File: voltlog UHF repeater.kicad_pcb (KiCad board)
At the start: 4 copper layers, 48.2 x 46.2 mm, 38 parts, among them J1 Conn_02x13_Odd_Even, J2 Conn_01x13, J3 Conn_Coaxial, Q1 Q_NPN_BEC, Q2 Q_PNP_BEC, U1 SA818

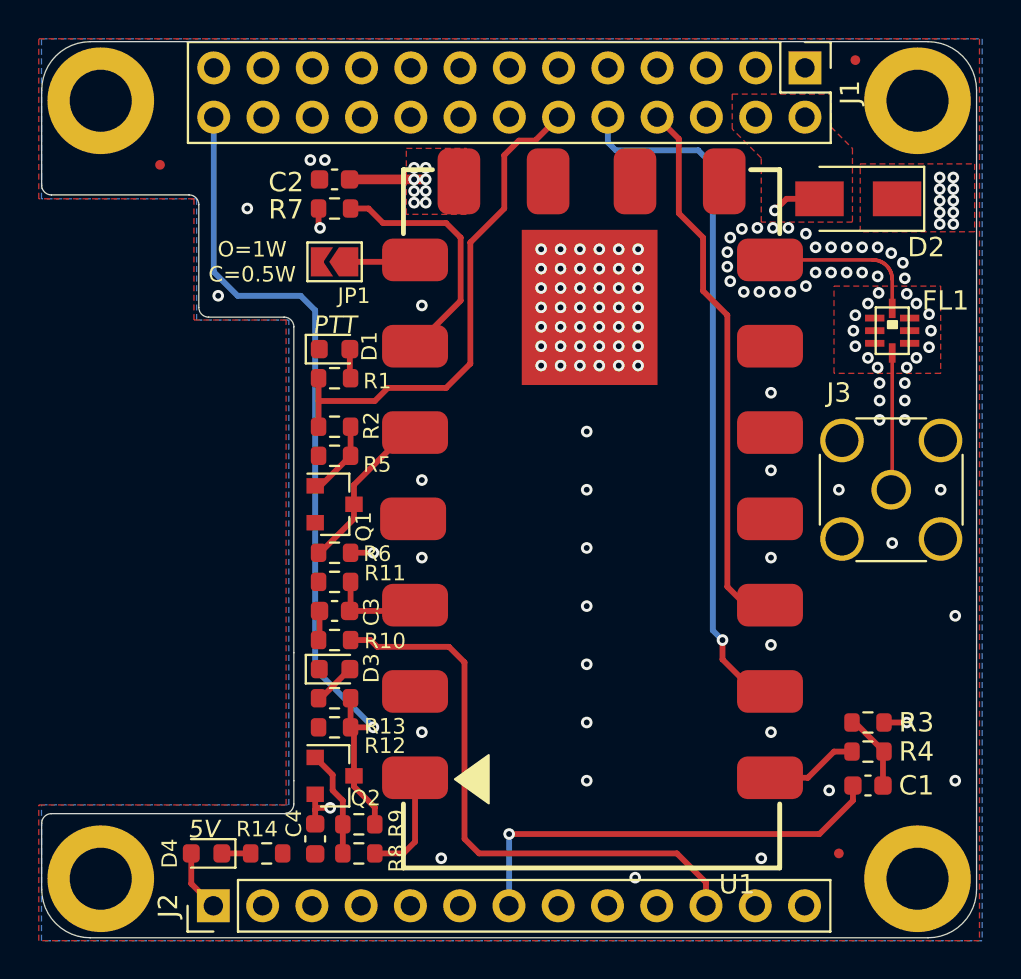
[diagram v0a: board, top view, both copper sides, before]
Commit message: Added pulldown for MIC1N. Added part no for JLCPCB and production files for JLCPCB.
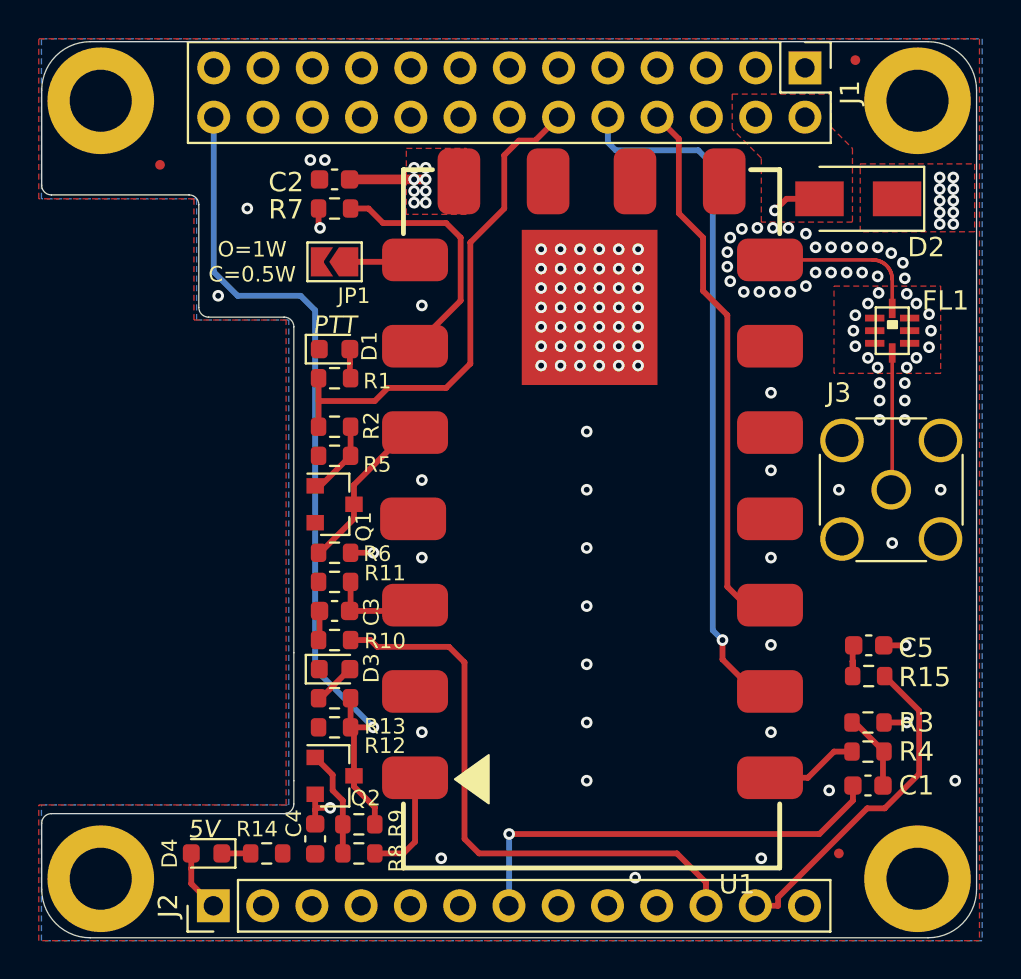
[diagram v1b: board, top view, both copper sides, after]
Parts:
- removed V1: VOLTLOG_LOGO, Voltlog:voltlog_mask_3mm
- added C5: 470nF, Capacitor_SMD:C_0603_1608Metric, F.Cu at (201.5, 65.0)
- added R15: 2K2, Resistor_SMD:R_0603_1608Metric, F.Cu at (201.5, 66.6)
- D1: value PTT -> LED
- D3: value SQL -> LED
- D4: value 5V -> LED
- Q1: value Q_NPN_BEC -> BC847
- Q2: value Q_PNP_BEC -> BC857
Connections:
- FL1 pad 2: Net-(FL1-Pad2) -> unconnected-(FL1-NC-Pad2)
- FL1 pad 6: Net-(FL1-Pad6) -> unconnected-(FL1-NC-Pad6)
- J2 pad 12: /MIC1N -> MIC1N
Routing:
- net MIC1N: track 0.00 -> 17.3 mm
- net Net-(C5-Pad1): track 0.00 -> 2.37 mm
- net GND: track 1.18 -> 2.31 mm
- net +5V: track 74.0 -> 74.8 mm
- net Net-(D1-A): track 1.46 -> 2.25 mm
- added copper zone on In1.Cu, net GND
- added copper zone on In2.Cu, net GND
- added copper zone on In2.Cu, net Net-(D2-K)
- removed copper zone on GND.Cu, net GND
- removed copper zone on PWR.Cu, net GND
- removed copper zone on PWR.Cu, net Net-(D2-K)
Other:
- net class 50ohm removed
- net class Default removed
- board text added: "revB"
- board text removed: "UHF"
- board text removed: "revA 3721"

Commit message: Fixed errors caused by orangepi outline present in Margin layer
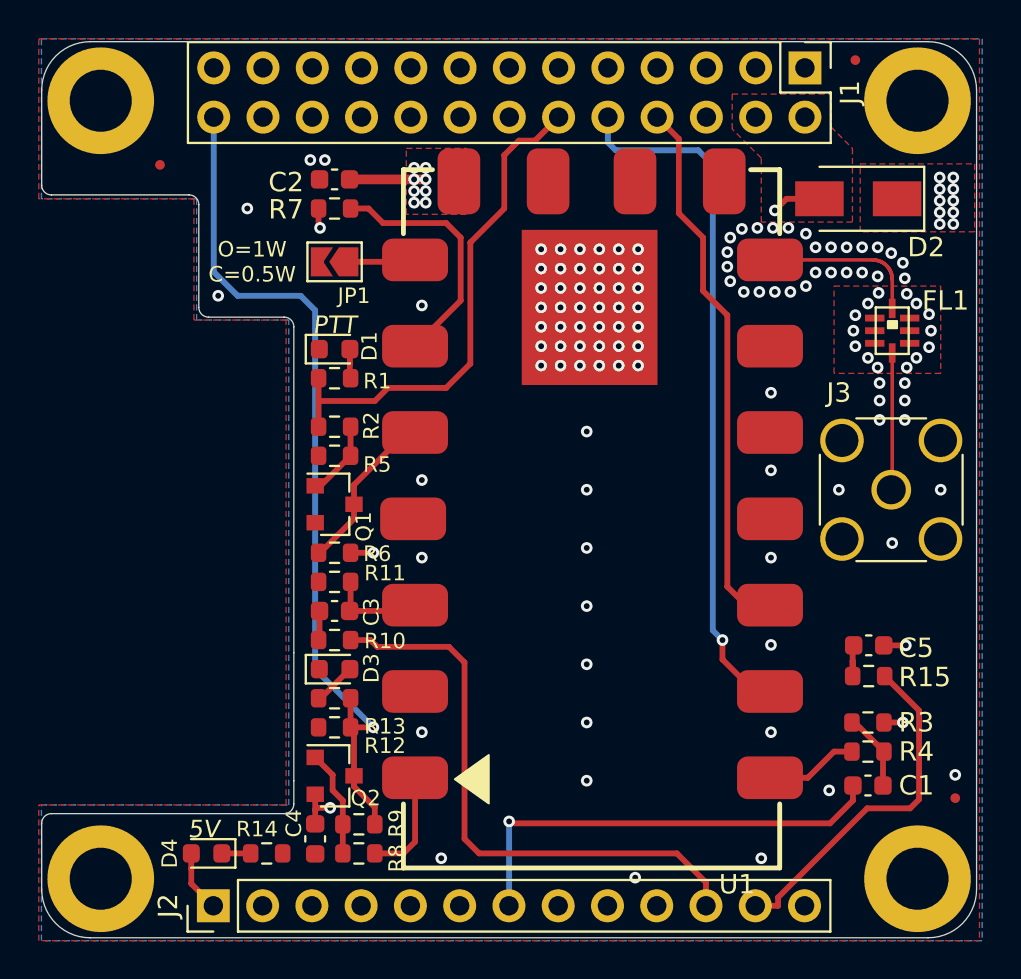
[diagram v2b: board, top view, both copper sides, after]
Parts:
- moved FID1 6.64 mm to (206.0, 72.9)
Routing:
- net MIC1N: track 17.3 -> 18.1 mm
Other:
- board text removed: "46.0"
- board text removed: "48.0"
- board text removed: "GND"
- board text removed: "RX"
- board text removed: "TX"
